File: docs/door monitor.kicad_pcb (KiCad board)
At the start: 2 copper layers, 48.9 x 30.5 mm, 11 parts, among them J1 USB_B_Mini, J2 Screw_Terminal_01x02, SW1 SW_Push, U1 LM2937xS, U2 ESP-01v090

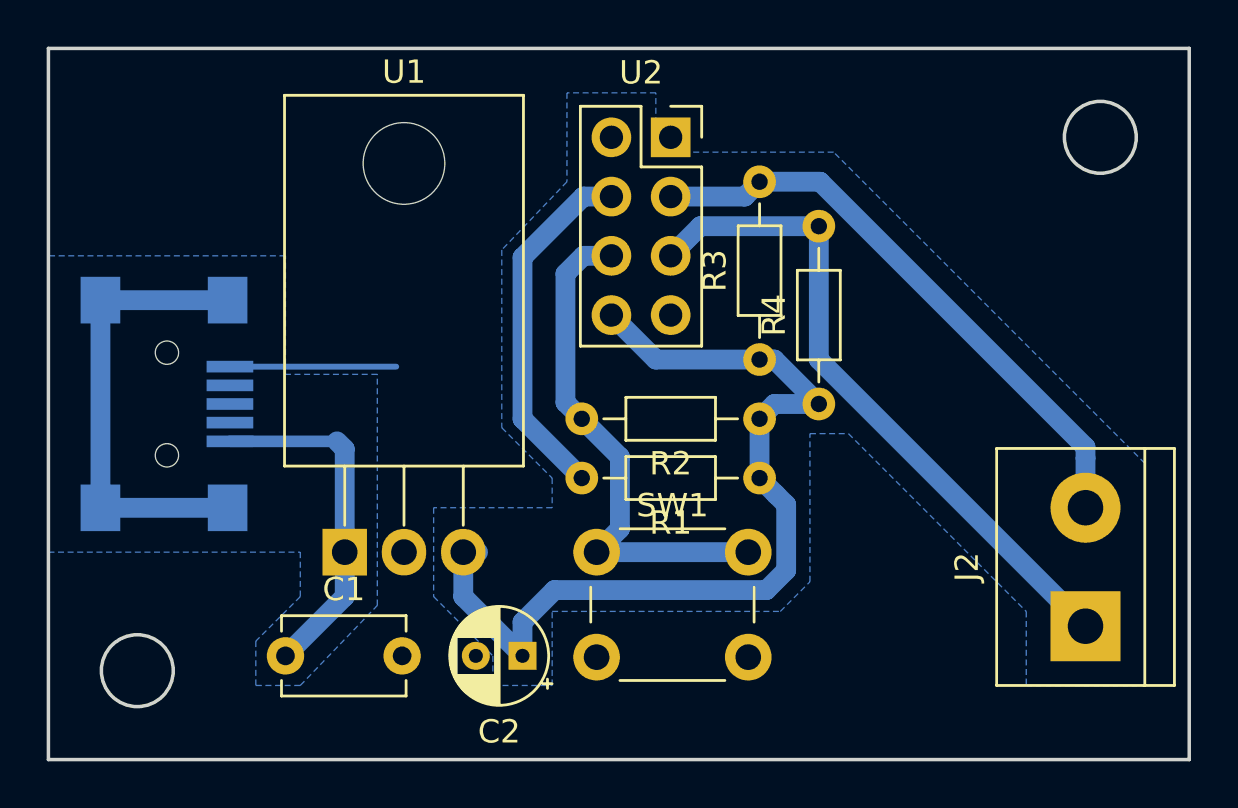
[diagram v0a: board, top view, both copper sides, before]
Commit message: Increase track space on PCB
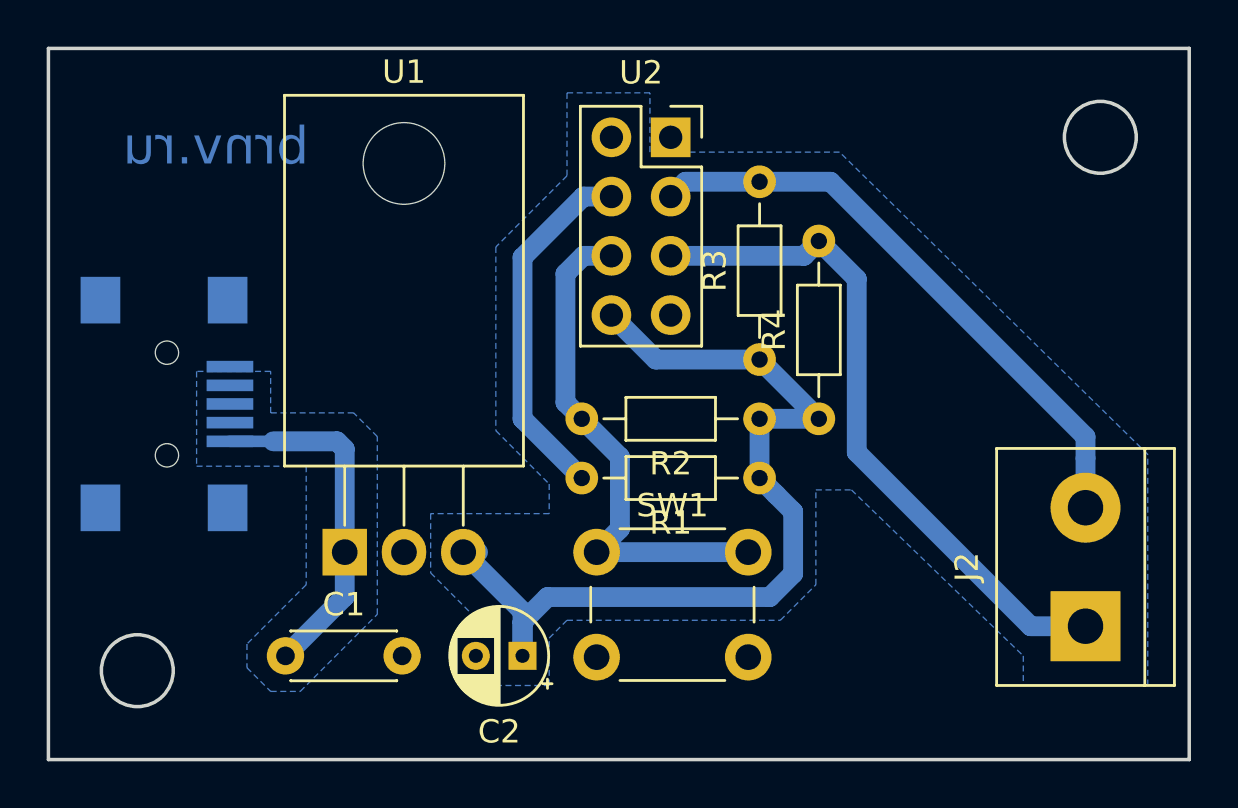
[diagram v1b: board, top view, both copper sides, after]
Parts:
- C1: footprint Capacitor_THT:C_Disc_D5.1mm_W3.2mm_P5.00mm -> Capacitor_THT:C_Disc_D4.3mm_W1.9mm_P5.00mm
- moved R4 0.64 mm to (159.4, 99.1)
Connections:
- J1 pad 6: Net-(J1-Pad6) -> Earth
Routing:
- net Net-(J1-Pad6): track 19.8 -> 0.00 mm
- net Earth: track 7.38 -> 0.25 mm
- net Net-(C2-Pad1): track 40.0 -> 40.5 mm
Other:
- net class Default: clearance 0.2 -> 0.5
- net class VCC added: clearance 0.2, trace_width 0.25, via_dia 0.8, via_drill 0.4
- rule trace_clearance: 0.2 -> 0.5
- board text added: "brnv.ru"
